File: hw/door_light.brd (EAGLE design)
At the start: 32.2 x 34.6 mm, 30 parts, among them IC1 TINY13-20SSU, Q1 BSP250, T1 n-mosfet, T2 KP-3216P3C, U1 MC33063ADE4

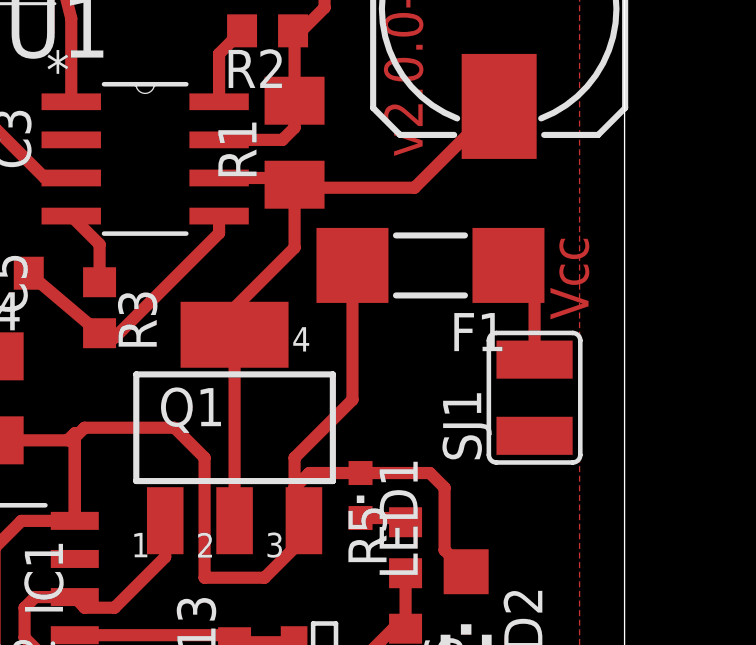
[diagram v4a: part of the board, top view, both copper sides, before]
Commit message: replaced on-bard big fuse with the smaller one (the one that has been actually bought)
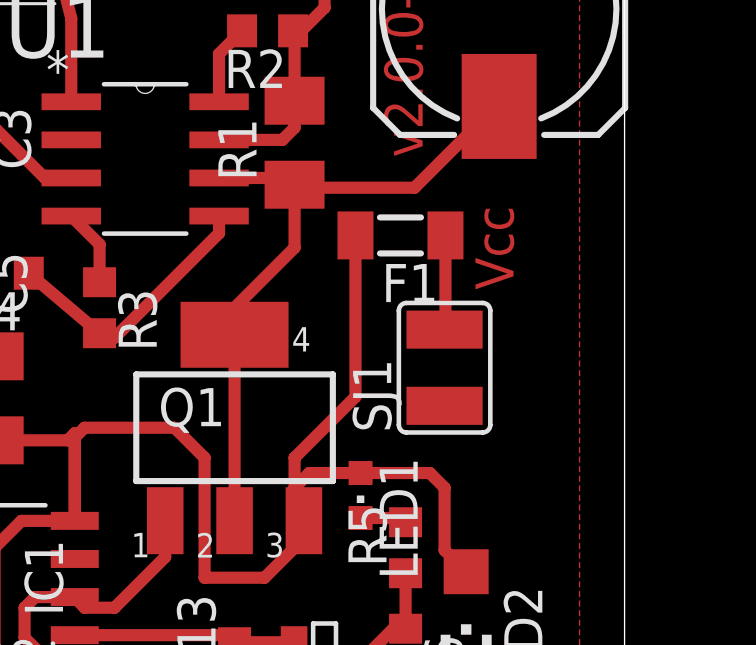
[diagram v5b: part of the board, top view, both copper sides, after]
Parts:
- F1: device rcl:MINI_MELF-0207W -> rcl:MINI_MELF-0204W
- moved SJ1 3.16 mm to (44.0, 54.0)
- moved F1 1.41 mm to (42.5, 58.4)
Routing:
- net N$8: track 4.66 -> 3.17 mm
- net +4.1V: track 63.3 -> 64.4 mm
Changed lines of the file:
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@@
 <wire x1="50" y1="74.38" x2="17.78" y2="74.38" width="0" layer="20"/>
 <wire x1="17.78" y1="74.38" x2="17.78" y2="39.75" width="0" layer="20"/>
-<text x="48.8" y="55.6" size="1.27" layer="1" rot="R90">Vcc</text>
+<text x="46.3" y="56.6" size="1.27" layer="1" rot="R90">Vcc</text>
 <text x="23.7" y="66.3" size="1.27" layer="1">L</text>
 <text x="42" y="69" size="1.27" layer="1" rot="R270">v2.0.0-rc5</text>
@@
 <attribute name="OC_FARNELL" value="1053588" x="34.02" y="60.96" size="1.778" layer="27" display="off"/>
 </element>
-<element name="F1" library="rcl" package="MINI_MELF-0207W" value="SD075-16 (F750mA)" x="43.53" y="57.41" rot="R180"/>
+<element name="F1" library="rcl" package="MINI_MELF-0204W" value="SD075-16 (F750mA)" x="42.53" y="58.41" rot="R180"/>
 <element name="R7" library="rcl" package="R0402" value="10kR" x="23.9" y="54.39" rot="R180"/>
 <element name="D1" library="diode" package="SMB" value=" MBRS140T3G" x="28.75" y="68.04"/>
@@
 <attribute name="OC_FARNELL" value="unknown" x="40" y="44" size="1.778" layer="27" rot="R90" display="off"/>
 </element>
-<element name="SJ1" library="jumper" package="SJW" value="PWR" x="47" y="53" rot="R90"/>
+<element name="SJ1" library="jumper" package="SJW" value="PWR" x="44" y="54" rot="R90"/>
 <element name="SJ2" library="jumper" package="SJW" value="LIGHT" x="22.4" y="69.5" rot="R180"/>
 <element name="R12" library="rcl" package="R0603" value="100kR" x="33.5" y="43" rot="R180"/>
@@
 <signal name="N$8">
 <contactref element="F1" pad="1"/>
-<wire x1="46.59" y1="56.95" x2="46.13" y2="57.41" width="0.4064" layer="1"/>
 <contactref element="SJ1" pad="2"/>
-<wire x1="47" y1="54.27" x2="47" y2="57" width="0.4064" layer="1"/>
-<wire x1="47" y1="57" x2="46.13" y2="57" width="0.4064" layer="1"/>
-<wire x1="46.13" y1="57" x2="46.13" y2="57.41" width="0.4064" layer="1"/>
+<wire x1="44" y1="55.27" x2="44.03" y2="55.27" width="0.4064" layer="1"/>
+<wire x1="44.03" y1="55.27" x2="44.03" y2="58.41" width="0.4064" layer="1"/>
 </signal>
 <signal name="+4.1V">
@@
 <contactref element="Q1" pad="3"/>
 <wire x1="31.674" y1="48.895" x2="31.674" y2="51.816" width="0.4064" layer="1"/>
-<wire x1="40.93" y1="57.41" x2="40.93" y2="52.93" width="0.4064" layer="1"/>
-<wire x1="40.93" y1="52.93" x2="39" y2="51" width="0.4064" layer="1"/>
+<wire x1="41.03" y1="53.03" x2="39" y2="51" width="0.4064" layer="1"/>
 <wire x1="39" y1="51" x2="39" y2="50" width="0.4064" layer="1"/>
 <wire x1="39" y1="50" x2="39" y2="49.2126" width="0.4064" layer="1"/>
@@
 <wire x1="29.07" y1="51.58" x2="27.42" y2="51.58" width="0.4064" layer="1"/>
 <wire x1="27.42" y1="51.58" x2="27" y2="52" width="0.4064" layer="1"/>
+<wire x1="41.03" y1="58.41" x2="41.03" y2="53.03" width="0.4064" layer="1"/>
 </signal>
 <signal name="N$10">
